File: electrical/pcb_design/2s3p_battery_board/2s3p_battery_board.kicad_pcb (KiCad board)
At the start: 2 copper layers, 82.5 x 82.5 mm, 28 parts, among them J1 2-pin Header, J2 2-pin Header, J3 2-pin Header, J4 2-pin Header, J5 504050-1091, J6 2-pin Header, U1 1043, U2 1043, U3 1043, U4 1043, U5 1043, U6 1043

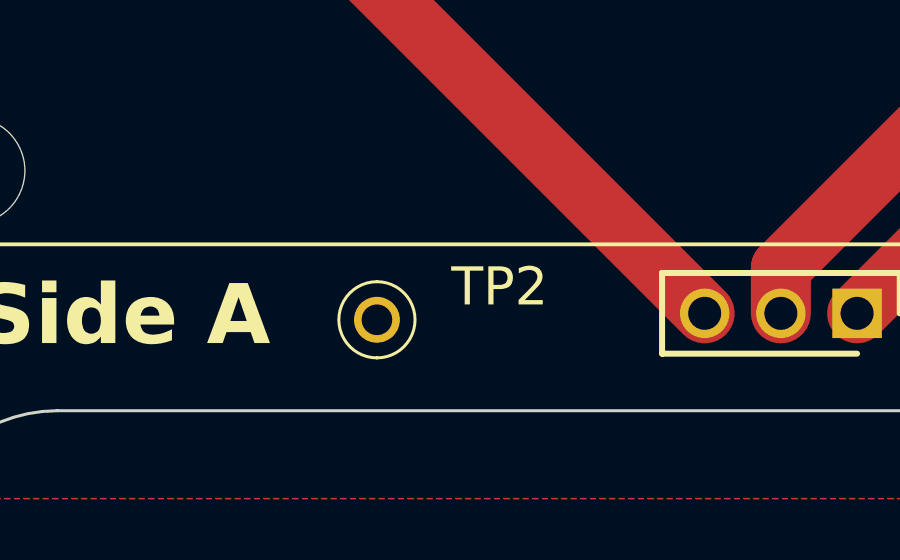
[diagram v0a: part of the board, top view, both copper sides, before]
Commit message: Clean up properties of some parts
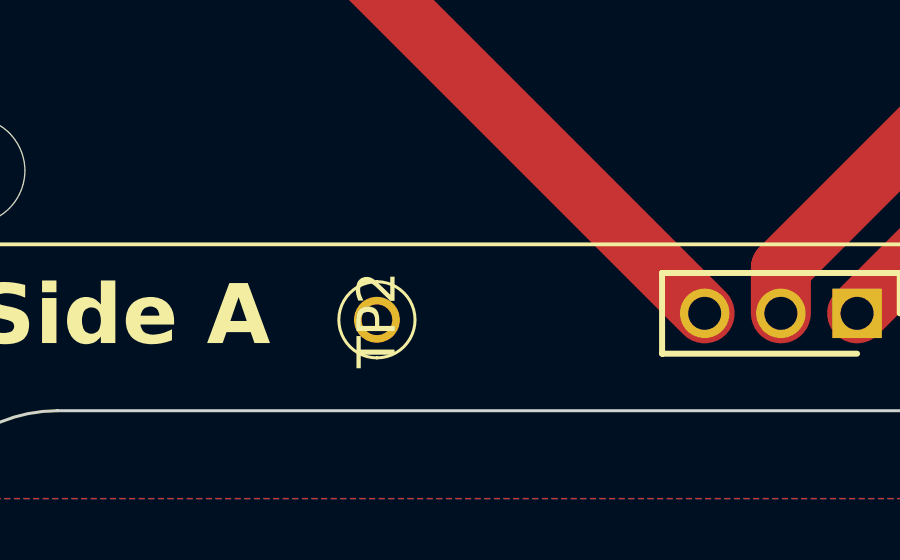
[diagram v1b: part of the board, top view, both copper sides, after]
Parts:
- TP2: footprint footprints:Keystone_5000 -> footprints:Keystone_5001
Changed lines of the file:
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@@
     (tags "Hardware")
     (property "Active" "Y")
+    (property "Color" "White")
     (property "MPN" "C238123")
     (property "Manufacturer" "Keystone")
@@
     (tags "Hardware")
     (property "Active" "Y")
+    (property "Color" "White")
     (property "MPN" "C238123")
     (property "Manufacturer" "Keystone")
@@
     )
   )
-  (footprint "footprints:Keystone_5000" (layer "F.Cu")
+  (footprint "footprints:Keystone_5001" (layer "F.Cu")
     (at 125.22 126.54 90)
-    (descr "5000-1")
+    (descr "5001-1")
     (tags "Hardware")
     (property "Active" "Y")
+    (property "Color" "Black")
     (property "MPN" "C238122")
     (property "Manufacturer" "Keystone")
@@
     (property "ki_keywords" "test point tp")
     (attr through_hole)
-    (fp_text reference "TP2" (at 1.1 4.09 180) (layer "F.SilkS")
-        (effects (font (size 1.27 1.27) (thickness 0.254)))
-    )
-    (fp_text value "Black" (at -0.392 -1.99 90) (layer "F.SilkS") hide
-        (effects (font (size 1.27 1.27) (thickness 0.254)))
-    )
-    (fp_text user "${REFERENCE}" (at 1.1 4.09 180) (layer "F.Fab")
+    (fp_text reference "TP2" (at 0 0 90) (layer "F.SilkS")
+        (effects (font (size 1.27 1.27) (thickness 0.254)))
+    )
+    (fp_text value "Black" (at 0 0 90) (layer "F.SilkS") hide
+        (effects (font (size 1.27 1.27) (thickness 0.254)))
+    )
+    (fp_text user "${REFERENCE}" (at 0 0 90) (layer "F.Fab")
         (effects (font (size 1.27 1.27) (thickness 0.254)))
     )
@@
     (pad "1" thru_hole circle (at 0 0 90) (size 1.53 1.53) (drill 1.02) (layers "*.Cu" "*.Mask")
       (net 2 "BATTERY_-") (pinfunction "1") (pintype "passive"))
-    (model "${KIPRJMOD}/../../3dmodels/Keystone_5000.step"
+    (model "${KIPRJMOD}/../../3dmodels/Keystone_5001.step"
       (offset (xyz 0 0 1.5))
       (scale (xyz 1 1 1))
@@
     (at 139 113.7)
     (property "Active" "Y")
-    (property "MANUFACTURER" "Keystone")
-    (property "MAXIMUM_PACKAGE_HEIGHT" "14.86mm")
-    (property "MPN" "")
+    (property "MPN" "C5355143")
     (property "Manufacturer" "Keystone")
     (property "Manufacturer Part Number" "1043")
-    (property "PARTREV" "J")
-    (property "Purpose" "")
-    (property "SNAPEDA_PN" "1043")
-    (property "STANDARD" "Manufacturer Recommendations")
     (property "Sheetfile" "2s3p_battery_board.kicad_sch")
     (property "Sheetname" "")
@@
     (tags "Hardware")
     (property "Active" "Y")
+    (property "Color" "White")
     (property "MPN" "C238123")
     (property "Manufacturer" "Keystone")
@@
     (at 139 92.4)
     (property "Active" "Y")
-    (property "MANUFACTURER" "Keystone")
-    (property "MAXIMUM_PACKAGE_HEIGHT" "14.86mm")
-    (property "MPN" "")
+    (property "MPN" "C5355143")
     (property "Manufacturer" "Keystone")
     (property "Manufacturer Part Number" "1043")
-    (property "PARTREV" "J")
-    (property "Purpose" "")
-    (property "SNAPEDA_PN" "1043")
-    (property "STANDARD" "Manufacturer Recommendations")
     (property "Sheetfile" "2s3p_battery_board.kicad_sch")
     (property "Sheetname" "")
@@
     (tags "Hardware")
     (property "Active" "Y")
+    (property "Color" "Red")
     (property "MPN" "C5199900")
     (property "Manufacturer" "Keystone")
@@
     (at 139 71.1)
     (property "Active" "Y")
-    (property "MANUFACTURER" "Keystone")
-    (property "MAXIMUM_PACKAGE_HEIGHT" "14.86mm")
-    (property "MPN" "")
+    (property "MPN" "C5355143")
     (property "Manufacturer" "Keystone")
     (property "Manufacturer Part Number" "1043")
-    (property "PARTREV" "J")
-    (property "Purpose" "")
-    (property "SNAPEDA_PN" "1043")
-    (property "STANDARD" "Manufacturer Recommendations")
     (property "Sheetfile" "2s3p_battery_board.kicad_sch")
     (property "Sheetname" "")
@@
     (at 143.5 90.1 180)
     (property "Active" "Y")
-    (property "MANUFACTURER" "Keystone")
-    (property "MAXIMUM_PACKAGE_HEIGHT" "14.86mm")
-    (property "MPN" "")
+    (property "MPN" "C5355143")
     (property "Manufacturer" "Keystone")
     (property "Manufacturer Part Number" "1043")
-    (property "PARTREV" "J")
-    (property "Purpose" "")
-    (property "SNAPEDA_PN" "1043")
-    (property "STANDARD" "Manufacturer Recommendations")
     (property "Sheetfile" "2s3p_battery_board.kicad_sch")
     (property "Sheetname" "")
@@
     (at 143.5 68.8 180)
     (property "Active" "Y")
-    (property "MANUFACTURER" "Keystone")
-    (property "MAXIMUM_PACKAGE_HEIGHT" "14.86mm")
-    (property "MPN" "")
+    (property "MPN" "C5355143")
     (property "Manufacturer" "Keystone")
     (property "Manufacturer Part Number" "1043")
-    (property "PARTREV" "J")
-    (property "Purpose" "")
-    (property "SNAPEDA_PN" "1043")
-    (property "STANDARD" "Manufacturer Recommendations")
     (property "Sheetfile" "2s3p_battery_board.kicad_sch")
     (property "Sheetname" "")
@@
     (at 143.5 111.4 180)
     (property "Active" "Y")
-    (property "MANUFACTURER" "Keystone")
-    (property "MAXIMUM_PACKAGE_HEIGHT" "14.86mm")
-    (property "MPN" "")
+    (property "MPN" "C5355143")
     (property "Manufacturer" "Keystone")
     (property "Manufacturer Part Number" "1043")
-    (property "PARTREV" "J")
-    (property "Purpose" "")
-    (property "SNAPEDA_PN" "1043")
-    (property "STANDARD" "Manufacturer Recommendations")
-    (property "Sheetfile" "2s3p_battery_board.kicad_sch")
-    (property "Sheetname" "")
+    (property "Sheetfile" "2s3p_battery_board.kicad_sch")
+    (property "Sheetname" "")

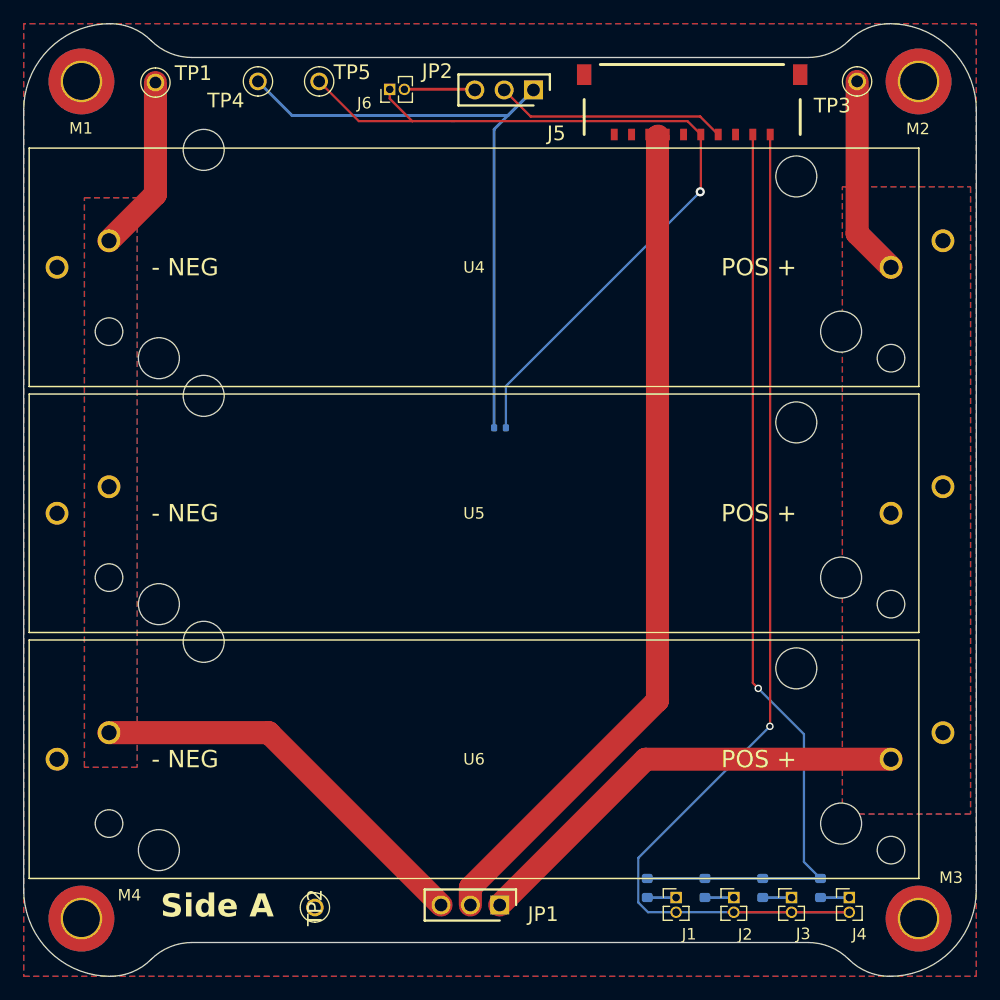
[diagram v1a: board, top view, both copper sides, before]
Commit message: Fixed major bug where header orientations need to be swapped on different ends of the cabling.
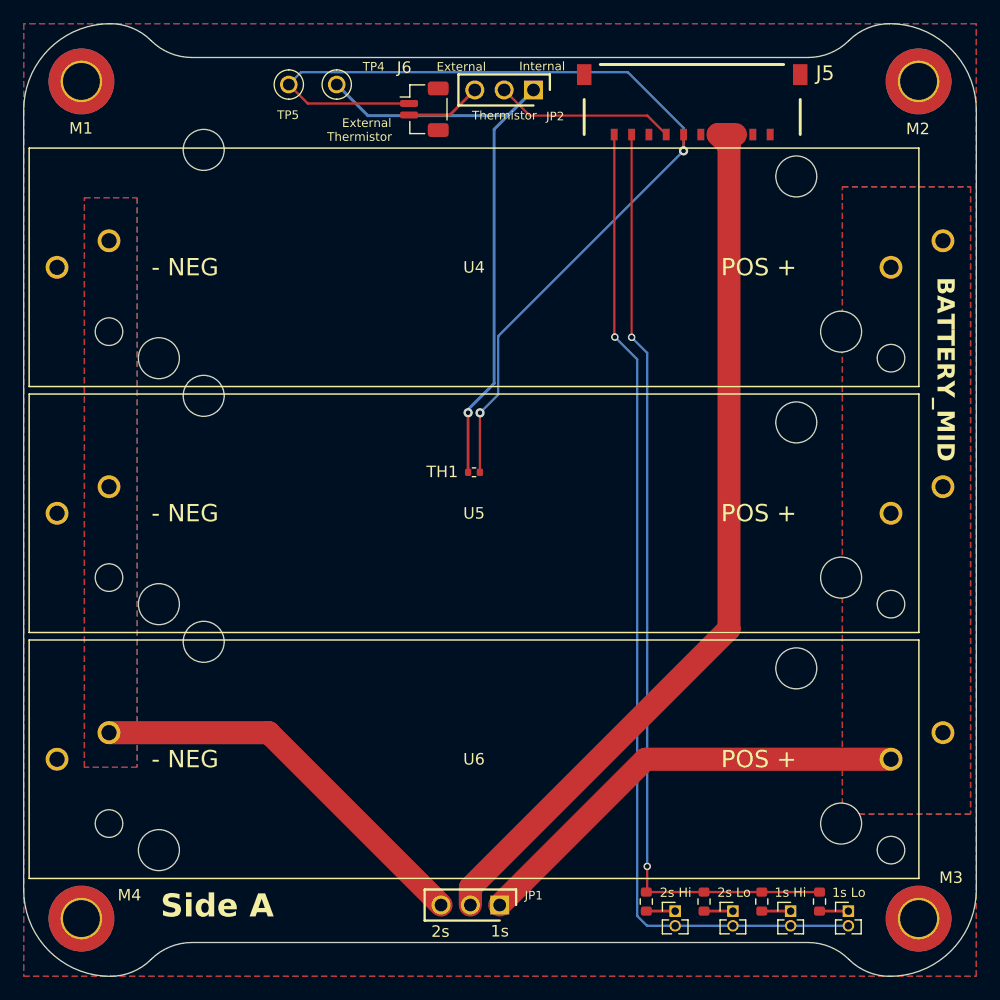
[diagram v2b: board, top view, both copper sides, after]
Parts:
- removed TP1: Red, footprints:Keystone_5000
- removed TP2: Black, footprints:Keystone_5001
- removed TP3: White, footprints:Keystone_5002
- J5: value 504050-1091 -> Interconnect_Battery_Power-Battery_side
- J6: value 2-pin Header -> Conn_02x01_MountingPin; footprint Connector_PinHeader_1.27mm:PinHeader_1x02_P1.27mm_Vertical -> Connector_Molex:Molex_Pico-Clasp_501331-0207_1x02-1MP_P1.00mm_Vertical
- R1, R2, R3, R4, TH1: moved to F.Cu
- moved TP4 6.83 mm to (127.1, 55.3)
- moved TH1 4.46 mm to (139.0, 88.8)
- moved J6 3.46 mm to (134.7, 57.4), turned to -90 degrees
- moved TP5 2.64 mm to (123.0, 55.3)
- moved R1 1.18 mm to (153.9, 126.0)
- moved R2 1.18 mm to (158.9, 126.0)
- moved R3 1.18 mm to (163.9, 126.0)
- moved R4 1.18 mm to (168.9, 126.0)
- moved J1 1.18 mm to (156.4, 126.9)
- moved J2 1.18 mm to (161.4, 126.9)
- moved J3 1.18 mm to (166.4, 126.9)
- moved J4 1.18 mm to (171.4, 126.9)
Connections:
- J5 pad 1: BATTERY_- -> BATTERY_ID_+
- J5 pad 10: BATTERY_ID_+ -> BATTERY_-
- J5 pad 2: BATTERY_- -> BATTERY_ID_-
- J5 pad 3: /BATTERY_+_OUTPUT -> unconnected-(J5-UNUSED-Pad3)
- J5 pad 4: /BATTERY_+_OUTPUT -> THERMISTOR_+
- J5 pad 5: unconnected-(J5-Pad5) -> THERMISTOR_-
- J5 pad 6: THERMISTOR_- -> unconnected-(J5-UNUSED-Pad6)
- J5 pad 7: THERMISTOR_+ -> /BATTERY_+_OUTPUT
- J5 pad 8: unconnected-(J5-Pad8) -> /BATTERY_+_OUTPUT
- J5 pad 9: BATTERY_ID_- -> BATTERY_-
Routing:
- net BATTERY_MID: track 56.4 -> 39.1 mm
- net BATTERY_+: track 50.3 -> 34.9 mm
- net THERMISTOR_-: track 70.9 -> 86.3 mm, vias 1 -> 2
- net BATTERY_ID_+: track 100.4 -> 87.1 mm
- net THERMISTOR_+: track 20.1 -> 15.6 mm
- net /BATTERY_+_OUTPUT: track 75.5 -> 77.9 mm
- net /THERMISTOR_REAL_+: track 56.7 -> 54.5 mm, vias 0 -> 1
- net BATTERY_ID_-: track 81.9 -> 81.2 mm, vias 1 -> 2
- net Net-(J6-Pin_2): track 6.13 -> 6.68 mm
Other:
- board text added: "BATTERY_MID"
